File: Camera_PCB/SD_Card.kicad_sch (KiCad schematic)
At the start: 7 parts

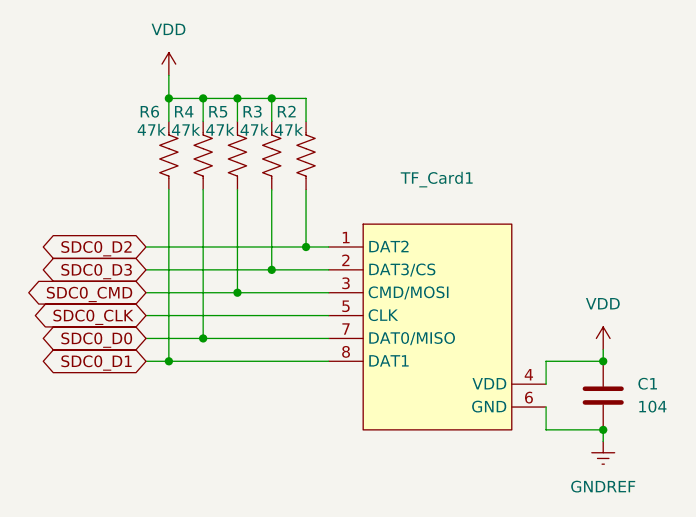
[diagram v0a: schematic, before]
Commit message: Fixed Capacitor Naming
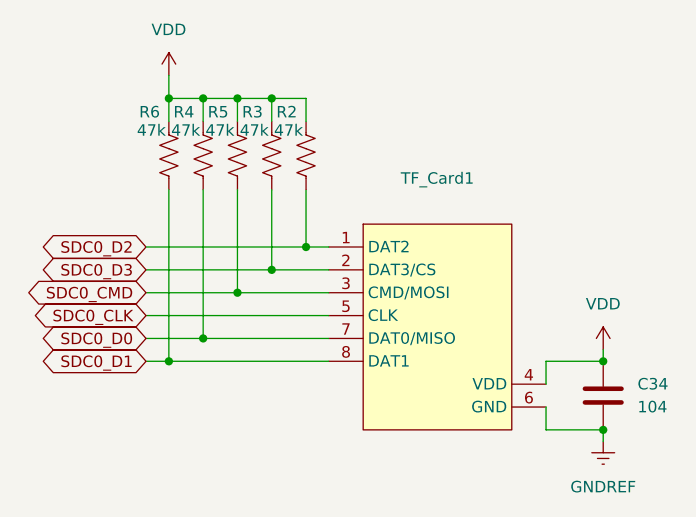
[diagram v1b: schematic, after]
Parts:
- renumbered C1 to C34
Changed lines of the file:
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@@
 		(dnp no)
 		(fields_autoplaced yes)
-		(property "Reference" "C1"
+		(property "Reference" "C34"
 			(at 175.26 96.5199 0)
 			(effects
@@
 			(project ""
 				(path "/400c1603-202c-4359-a830-d2f0d06dd3ce/a4c77a59-a27d-4681-b324-24cee2a545f5"
-					(reference "C1")
+					(reference "C34")
 					(unit 1)
 				)

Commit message: Switched pins 86, 87
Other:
- company: (none) -> Group 25 Senior Design
- title: (none) -> Wireless Backup Camera - Encoder
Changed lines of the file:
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@@
 	(generator_version "9.0")
 	(paper "A4")
+	(title_block
+		(title "Wireless Backup Camera - Encoder")
+		(company "Group 25 Senior Design")
+	)
 	(junction
 		(at 171.45 93.98)

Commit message: Started PCB
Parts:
- C34: footprint (none) -> Capacitor_SMD:C_0805_2012Metric_Pad1.18x1.45mm_HandSolder
- R2, R3, R4, R5, R6: footprint (none) -> Resistor_SMD:R_0805_2012Metric_Pad1.20x1.40mm_HandSolder
- TF_Card1: footprint (none) -> Connector_Card:microSD_HC_Hirose_DM3D-SF
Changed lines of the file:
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@@
 			)
 		)
-		(property "Footprint" ""
+		(property "Footprint" "Connector_Card:microSD_HC_Hirose_DM3D-SF"
 			(at 149.86 85.09 0)
 			(effects
@@
 			)
 		)
-		(property "Footprint" ""
+		(property "Footprint" "Capacitor_SMD:C_0805_2012Metric_Pad1.18x1.45mm_HandSolder"
 			(at 172.4152 101.6 0)
 			(effects
@@
 			)
 		)
-		(property "Footprint" ""
+		(property "Footprint" "Resistor_SMD:R_0805_2012Metric_Pad1.20x1.40mm_HandSolder"
 			(at 124.206 71.374 90)
 			(effects
@@
 			)
 		)
-		(property "Footprint" ""
+		(property "Footprint" "Resistor_SMD:R_0805_2012Metric_Pad1.20x1.40mm_HandSolder"
 			(at 139.446 71.374 90)
 			(effects
@@
 			)
 		)
-		(property "Footprint" ""
+		(property "Footprint" "Resistor_SMD:R_0805_2012Metric_Pad1.20x1.40mm_HandSolder"
 			(at 135.636 71.374 90)
 			(effects
@@
 			)
 		)
-		(property "Footprint" ""
+		(property "Footprint" "Resistor_SMD:R_0805_2012Metric_Pad1.20x1.40mm_HandSolder"
 			(at 128.016 71.374 90)
 			(effects
@@
 			)
 		)
-		(property "Footprint" ""
+		(property "Footprint" "Resistor_SMD:R_0805_2012Metric_Pad1.20x1.40mm_HandSolder"
 			(at 131.826 71.374 90)
 			(effects

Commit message: cleaned up PCB branch
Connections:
- net GNDREF renamed GND
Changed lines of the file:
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@@
+	)
+	(symbol
+		(lib_id "power:GND")
+		(at 171.45 102.87 0)
+		(unit 1)
+		(exclude_from_sim no)
+		(in_bom yes)
+		(on_board yes)
+		(dnp no)
+		(fields_autoplaced yes)
+		(property "Reference" "#PWR02"
+			(at 171.45 109.22 0)
+			(effects
+				(font
+					(size 1.27 1.27)
+				)
+				(hide yes)
+			)
+		)
+		(property "Value" "GND"
+			(at 171.45 107.95 0)
+			(effects
+				(font
+					(size 1.27 1.27)
+				)
+			)
+		)
+		(property "Footprint" ""
+			(at 171.45 102.87 0)
+			(effects
+				(font
+					(size 1.27 1.27)
+				)
+				(hide yes)
+			)
+		)
+		(property "Datasheet" ""
+			(at 171.45 102.87 0)
+			(effects
+				(font
+					(size 1.27 1.27)
+				)
+				(hide yes)
+			)
+		)
+		(property "Description" "Power symbol creates a global label with name \"GND\" , ground"
+			(at 171.45 102.87 0)
+			(effects
+				(font
+					(size 1.27 1.27)
+				)
+				(hide yes)
+			)
+		)
+		(pin "1"
+		)
+		(instances
+			(project ""
+				(path "/400c1603-202c-4359-a830-d2f0d06dd3ce/a4c77a59-a27d-4681-b324-24cee2a545f5"
+					(reference "#PWR02")
+					(unit 1)
+				)
+			)
+		)
 	)
 	(symbol
@@
 					(unit 1)
 				)
-			)
-		)
-	)
-	(symbol
-		(lib_id "power:GNDREF")
-		(at 171.45 102.87 0)
-		(unit 1)
-		(exclude_from_sim no)
-		(in_bom yes)
-		(on_board yes)
-		(dnp no)
-		(fields_autoplaced yes)
-		(property "Reference" "#PWR02"
-			(at 171.45 109.22 0)
-			(effects
-				(font
-					(size 1.27 1.27)
-				)
-				(hide yes)
-			)
-		)
-		(property "Value" "GNDREF"
-			(at 171.45 107.95 0)
-			(effects
-				(font
-					(size 1.27 1.27)
-				)
-			)
-		)
-		(property "Footprint" ""
-			(at 171.45 102.87 0)
-			(effects
-				(font
-					(size 1.27 1.27)
-				)
-				(hide yes)
-			)
-		)
-		(property "Datasheet" ""
-			(at 171.45 102.87 0)
-			(effects
-				(font
-					(size 1.27 1.27)
-				)
-				(hide yes)
-			)
-		)
-		(property "Description" "Power symbol creates a global label with name \"GNDREF\" , reference supply ground"
-			(at 171.45 102.87 0)
-			(effects
-				(font
-					(size 1.27 1.27)
-				)
-				(hide yes)
-			)
-		)
-		(pin "1"
-		)
-		(instances
-			(project ""
-				(path "/400c1603-202c-4359-a830-d2f0d06dd3ce/a4c77a59-a27d-4681-b324-24cee2a545f5"
-					(reference "#PWR02")
-					(unit 1)
-				)
